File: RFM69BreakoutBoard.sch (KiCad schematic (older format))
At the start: 22 parts, among them P1 CONN_7, P10 TST, P2 TST, P3 TST, P4 TST, P5 TST, P6 TST, P7 TST, P8 TST, P9 TST, U1 MCP1703, U2 74LVC245, U3 RFM69HW

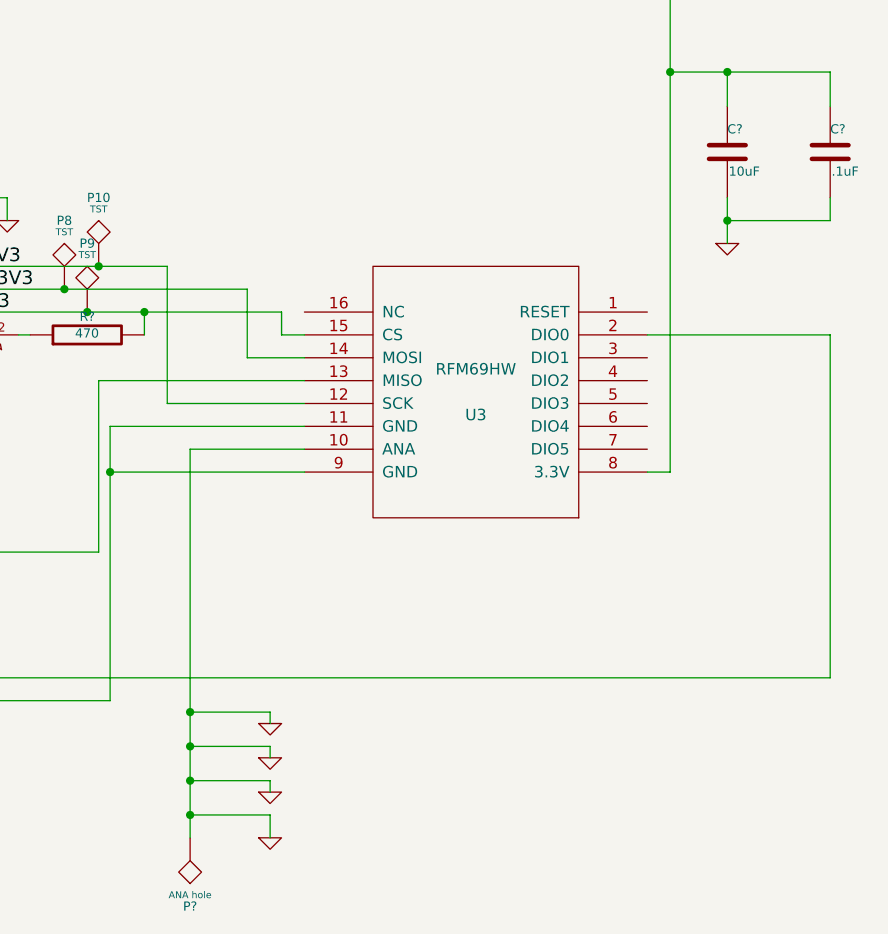
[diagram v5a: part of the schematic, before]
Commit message: changed cap near rfm69hw to 47uF, modified ANA pin
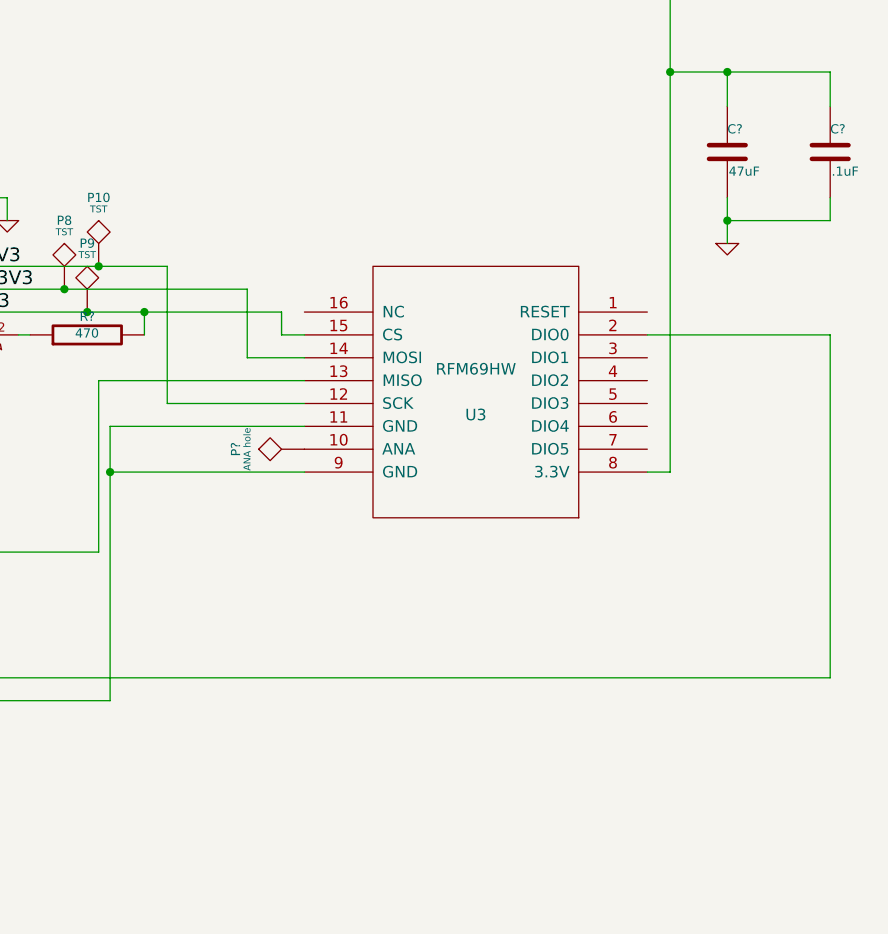
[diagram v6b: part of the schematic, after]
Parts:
- C?: value 10uF -> 47uF
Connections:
- wire segments 89 -> 79
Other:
- moved on the sheet: P?
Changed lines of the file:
@@
 P 10100 3650
 F 0 "C?" H 10100 3750 40  0000 L CNN
-F 1 "10uF" H 10106 3565 40  0000 L CNN
+F 1 "47uF" H 10106 3565 40  0000 L CNN
 F 2 "~" H 10138 3500 30  0000 C CNN
 F 3 "~" H 10100 3650 60  0000 C CNN
@@
 L TST P?
 U 1 1 530E5A0D
-P 7750 6650
-F 0 "P?" H 7750 6950 40  0000 C CNN
-F 1 "ANA hole" H 7750 6900 30  0000 C CNN
-F 2 "~" H 7750 6650 60  0000 C CNN
-F 3 "~" H 7750 6650 60  0000 C CNN
-	1    7750 6650
-	-1   0    0    1
-$EndComp
-Wire Wire Line
-	8250 4950 7750 4950
-Wire Wire Line
-	7750 4950 7750 6650
-$Comp
-L GND #PWR?
-U 1 1 530E5AC0
-P 8100 6450
-F 0 "#PWR?" H 8100 6450 30  0001 C CNN
-F 1 "GND" H 8100 6380 30  0001 C CNN
-F 2 "" H 8100 6450 60  0000 C CNN
-F 3 "" H 8100 6450 60  0000 C CNN
-	1    8100 6450
-	1    0    0    -1
-$EndComp
-Wire Wire Line
-	7750 6400 8100 6400
-Wire Wire Line
-	8100 6400 8100 6450
-Connection ~ 7750 6400
-$Comp
-L GND #PWR?
-U 1 1 530E5B36
-P 8100 6300
-F 0 "#PWR?" H 8100 6300 30  0001 C CNN
-F 1 "GND" H 8100 6230 30  0001 C CNN
-F 2 "" H 8100 6300 60  0000 C CNN
-F 3 "" H 8100 6300 60  0000 C CNN
-	1    8100 6300
-	1    0    0    -1
-$EndComp
-Wire Wire Line
-	7750 6250 8100 6250
-Connection ~ 7750 6250
-$Comp
-L GND #PWR?
-U 1 1 530E5BAF
-P 8100 6150
-F 0 "#PWR?" H 8100 6150 30  0001 C CNN
-F 1 "GND" H 8100 6080 30  0001 C CNN
-F 2 "" H 8100 6150 60  0000 C CNN
-F 3 "" H 8100 6150 60  0000 C CNN
-	1    8100 6150
-	1    0    0    -1
-$EndComp
-Wire Wire Line
-	7750 6100 8100 6100
-Connection ~ 7750 6100
-Wire Wire Line
-	8100 6100 8100 6150
-Wire Wire Line
-	8100 6250 8100 6300
-$Comp
-L GND #PWR?
-U 1 1 530E5DE4
-P 8100 6650
-F 0 "#PWR?" H 8100 6650 30  0001 C CNN
-F 1 "GND" H 8100 6580 30  0001 C CNN
-F 2 "" H 8100 6650 60  0000 C CNN
-F 3 "" H 8100 6650 60  0000 C CNN
-	1    8100 6650
-	1    0    0    -1
-$EndComp
-Wire Wire Line
-	7750 6550 8100 6550
-Wire Wire Line
-	8100 6550 8100 6650
-Connection ~ 7750 6550
+P 8250 4950
+F 0 "P?" H 8250 5250 40  0000 C CNN
+F 1 "ANA hole" H 8250 5200 30  0000 C CNN
+F 2 "~" H 8250 4950 60  0000 C CNN
+F 3 "~" H 8250 4950 60  0000 C CNN
+	1    8250 4950
+	0    -1   -1   0
+$EndComp
 $EndSCHEMATC

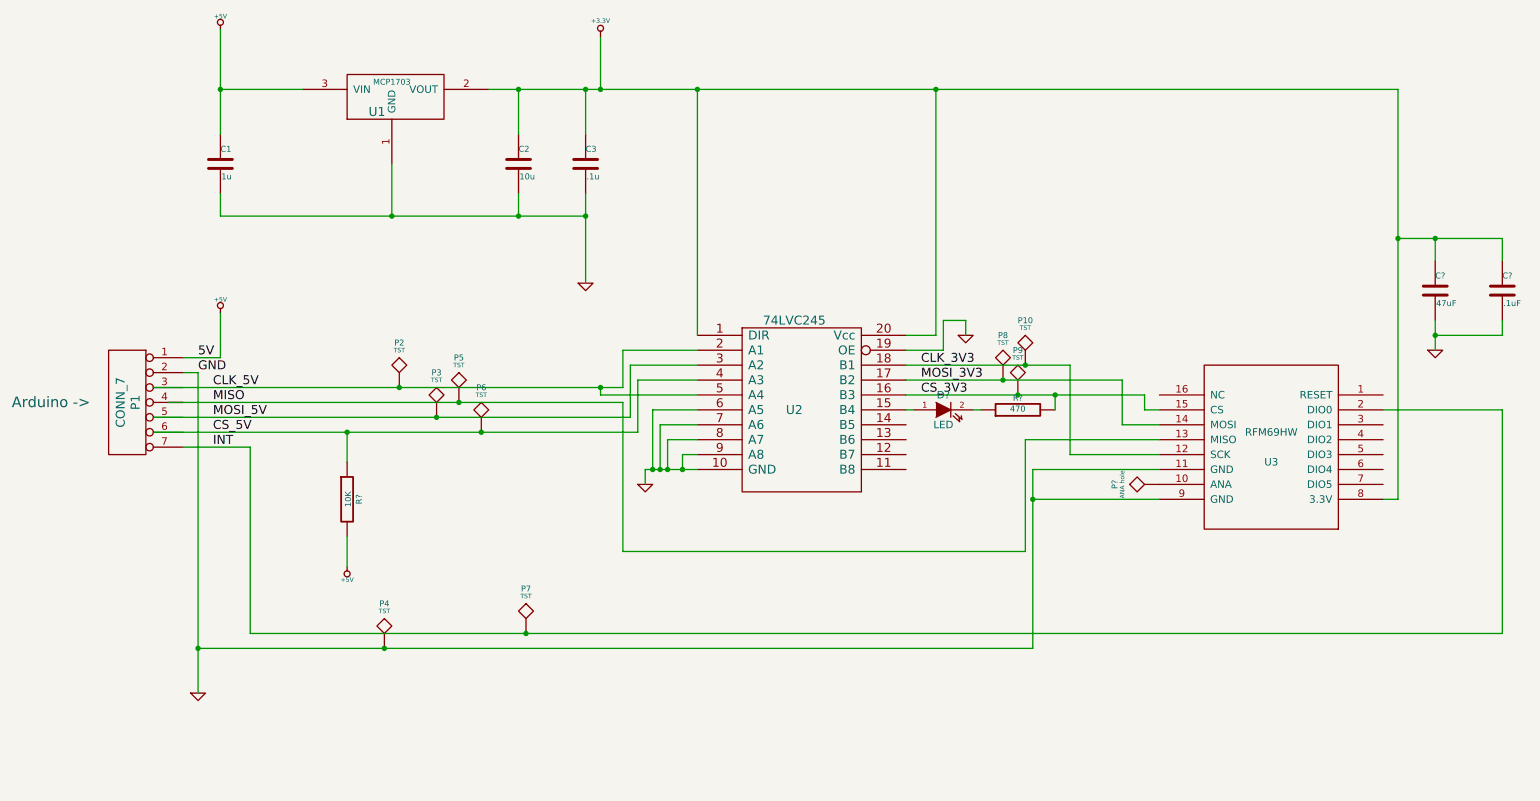
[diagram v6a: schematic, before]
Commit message: replaced larger caps to be electrolytic caps in the schematic
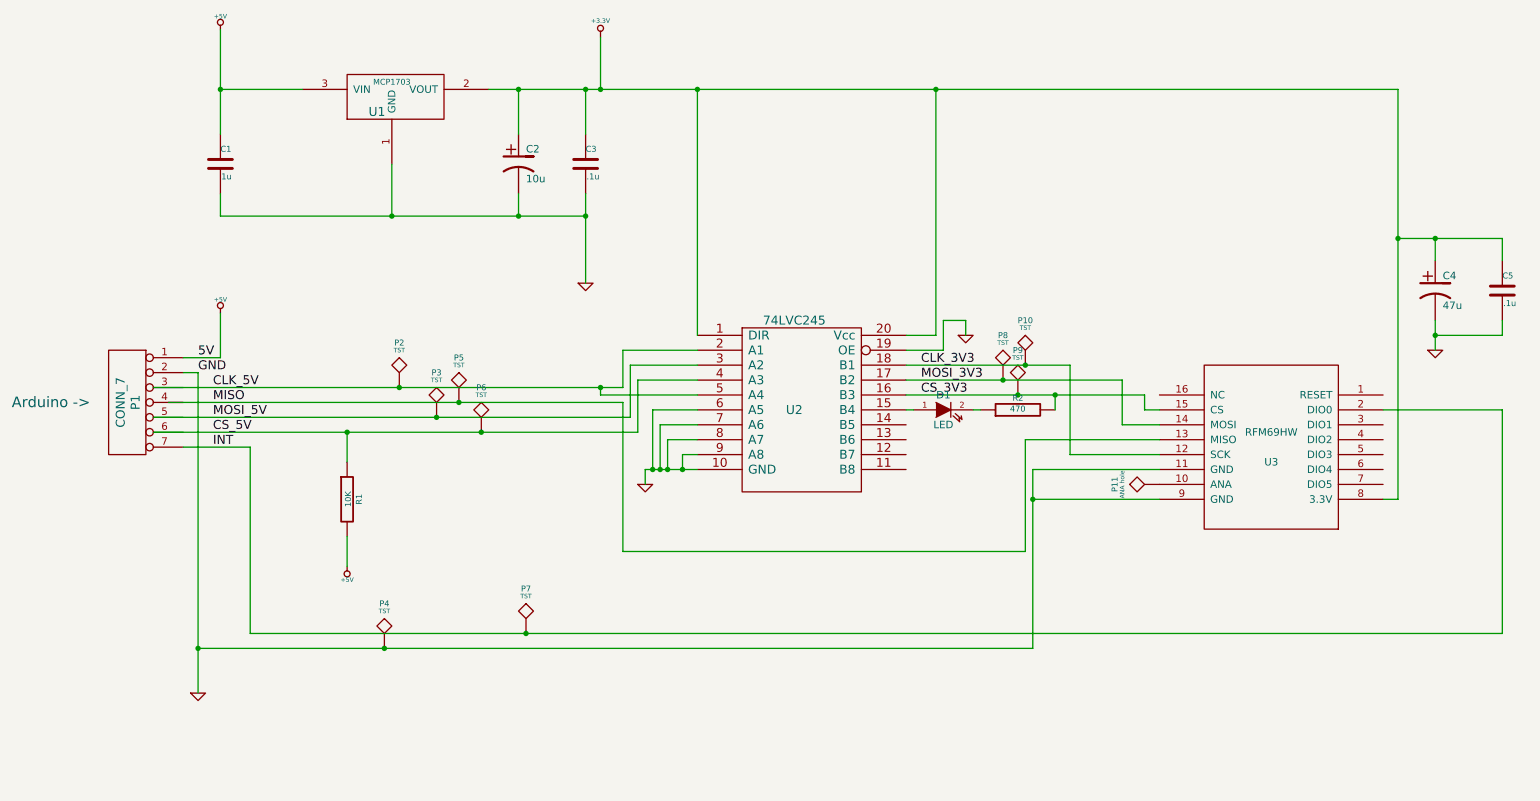
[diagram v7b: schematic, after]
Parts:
- removed C2: 10u, ~, symbol C
- removed C?: 47uF, ~, symbol C
- added C2: 10u, ~, symbol CP1
- added C4: 47u, ~, symbol CP1
- C5: renamed from C?; value .1uF -> .1u
- gave numbers to parts that had none: 4
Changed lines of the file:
@@
 Sheet 1 1
 Title ""
-Date "26 feb 2014"
+Date "27 feb 2014"
 Rev ""
 Comp ""
@@
 $EndComp
 $Comp
-L C C2
-U 1 1 5305B2AF
-P 3950 2800
-F 0 "C2" H 3950 2900 40  0000 L CNN
-F 1 "10u" H 3956 2715 40  0000 L CNN
-F 2 "~" H 3988 2650 30  0000 C CNN
-F 3 "~" H 3950 2800 60  0000 C CNN
-F 4 "Yageo" H 3950 2800 60  0001 C CNN "MFG Name"
-F 5 "CC0805ZKY5V6BB106" H 3950 2800 60  0001 C CNN "MFG Part Number"
-F 6 "311-1355-1-ND" H 3950 2800 60  0001 C CNN "Distributor Part Number"
-F 7 "http://www.digikey.com/product-detail/en/CC0805ZKY5V6BB106/311-1355-1-ND/2103139" H 3950 2800 60  0001 C CNN "Distributor Part Number Link"
-	1    3950 2800
-	1    0    0    -1
-$EndComp
-$Comp
 L C C3
 U 1 1 5305B2B5
@@
 $EndComp
 $Comp
-L +3.3V #PWR5
+L +3.3V #PWR6
 U 1 1 5305B30B
 P 4500 1950
-F 0 "#PWR5" H 4500 1910 30  0001 C CNN
+F 0 "#PWR6" H 4500 1910 30  0001 C CNN
 F 1 "+3.3V" H 4500 2060 30  0000 C CNN
 F 2 "" H 4500 1950 60  0000 C CNN
@@
 $EndComp
 $Comp
-L GND #PWR4
+L GND #PWR5
 U 1 1 5305B481
 P 4400 3600
-F 0 "#PWR4" H 4400 3600 30  0001 C CNN
+F 0 "#PWR5" H 4400 3600 30  0001 C CNN
 F 1 "GND" H 4400 3530 30  0001 C CNN
 F 2 "" H 4400 3600 60  0000 C CNN
@@
 CS_3V3
 $Comp
-L GND #PWR6
+L GND #PWR7
 U 1 1 530BB7C1
 P 4800 4950
-F 0 "#PWR6" H 4800 4950 30  0001 C CNN
+F 0 "#PWR7" H 4800 4950 30  0001 C CNN
 F 1 "GND" H 4800 4880 30  0001 C CNN
 F 2 "" H 4800 4950 60  0000 C CNN
@@
 CLK_5V
 $Comp
-L GND #PWR7
+L GND #PWR8
 U 1 1 530BC03D
 P 6950 3950
-F 0 "#PWR7" H 6950 3950 30  0001 C CNN
+F 0 "#PWR8" H 6950 3950 30  0001 C CNN
 F 1 "GND" H 6950 3880 30  0001 C CNN
 F 2 "" H 6950 3950 60  0000 C CNN
@@
 $EndComp
 $Comp
-L R R?
+L R R2
 U 1 1 530DC938
 P 7300 4450
-F 0 "R?" V 7380 4450 40  0000 C CNN
+F 0 "R2" V 7380 4450 40  0000 C CNN
 F 1 "470" V 7307 4451 40  0000 C CNN
 F 2 "~" V 7230 4450 30  0000 C CNN
@@
 $EndComp
 $Comp
-L LED D?
+L LED D1
 U 1 1 530DC956
 P 6800 4450
-F 0 "D?" H 6800 4550 50  0000 C CNN
+F 0 "D1" H 6800 4550 50  0000 C CNN
 F 1 "LED" H 6800 4350 50  0000 C CNN
 F 2 "~" H 6800 4450 60  0000 C CNN
@@
 $EndComp
 $Comp
-L R R?
+L R R1
 U 1 1 530DCC1C
 P 2800 5050
-F 0 "R?" V 2880 5050 40  0000 C CNN
+F 0 "R1" V 2880 5050 40  0000 C CNN
 F 1 "10K" V 2807 5051 40  0000 C CNN
 F 2 "~" V 2730 5050 30  0000 C CNN
@@
 $EndComp
 $Comp
-L +5V #PWR?
+L +5V #PWR4
 U 1 1 530DCD57
 P 2800 5500
-F 0 "#PWR?" H 2800 5590 20  0001 C CNN
+F 0 "#PWR4" H 2800 5590 20  0001 C CNN
 F 1 "+5V" H 2800 5590 30  0000 C CNN
 F 2 "" H 2800 5500 60  0000 C CNN
@@
 $EndComp
 $Comp
-L C C?
-U 1 1 530DFDC0
-P 10100 3650
-F 0 "C?" H 10100 3750 40  0000 L CNN
-F 1 "47uF" H 10106 3565 40  0000 L CNN
-F 2 "~" H 10138 3500 30  0000 C CNN
-F 3 "~" H 10100 3650 60  0000 C CNN
-	1    10100 3650
-	1    0    0    -1
-$EndComp
-$Comp
-L GND #PWR?
+L GND #PWR9
 U 1 1 530DFEA1
 P 10100 4050
-F 0 "#PWR?" H 10100 4050 30  0001 C CNN
+F 0 "#PWR9" H 10100 4050 30  0001 C CNN
 F 1 "GND" H 10100 3980 30  0001 C CNN
 F 2 "" H 10100 4050 60  0000 C CNN
@@
 $EndComp
 $Comp
-L C C?
+L C C5
 U 1 1 530DFF22
 P 10550 3650
-F 0 "C?" H 10550 3750 40  0000 L CNN
-F 1 ".1uF" H 10556 3565 40  0000 L CNN
+F 0 "C5" H 10550 3750 40  0000 L CNN
+F 1 ".1u" H 10556 3565 40  0000 L CNN
 F 2 "~" H 10588 3500 30  0000 C CNN
 F 3 "~" H 10550 3650 60  0000 C CNN
@@
 Connection ~ 10100 3300
 $Comp
-L TST P?
+L TST P11
 U 1 1 530E5A0D
 P 8250 4950
-F 0 "P?" H 8250 5250 40  0000 C CNN
+F 0 "P11" H 8250 5250 40  0000 C CNN
 F 1 "ANA hole" H 8250 5200 30  0000 C CNN
 F 2 "~" H 8250 4950 60  0000 C CNN
@@
 	0    -1   -1   0
 $EndComp
+$Comp
+L CP1 C4
+U 1 1 530F2E03
+P 10100 3650
+F 0 "C4" H 10150 3750 50  0000 L CNN
+F 1 "47u" H 10150 3550 50  0000 L CNN
+F 2 "~" H 10100 3650 60  0000 C CNN
+F 3 "~" H 10100 3650 60  0000 C CNN
+	1    10100 3650
+	1    0    0    -1
+$EndComp
+$Comp
+L CP1 C2
+U 1 1 530F2E4A
+P 3950 2800
+F 0 "C2" H 4000 2900 50  0000 L CNN
+F 1 "10u" H 4000 2700 50  0000 L CNN
+F 2 "~" H 3950 2800 60  0000 C CNN
+F 3 "~" H 3950 2800 60  0000 C CNN
+	1    3950 2800
+	1    0    0    -1
+$EndComp
 $EndSCHEMATC

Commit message: updated schema: changed 47uF cap to 10uF. Changed test point symbol
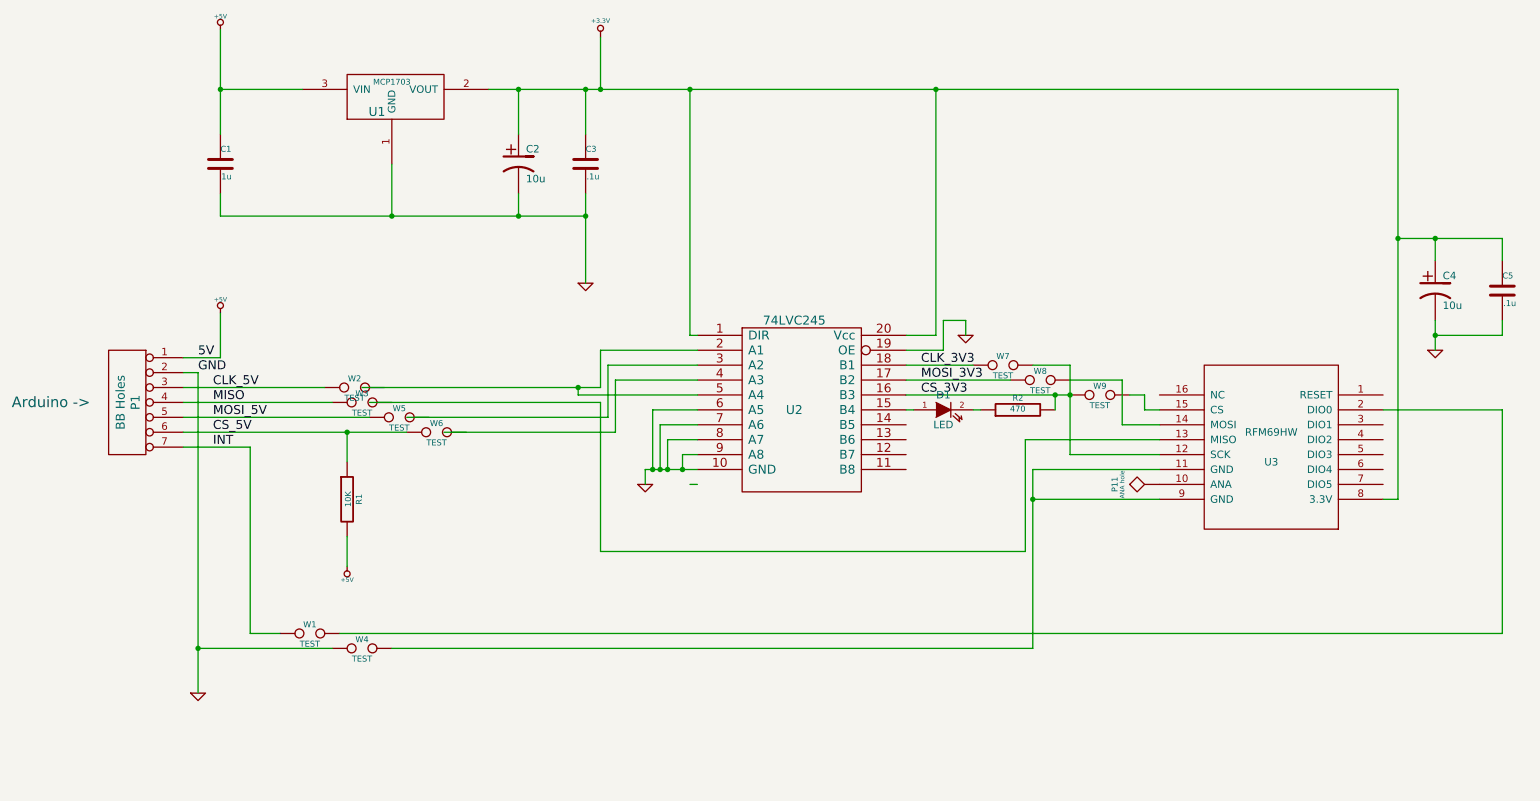
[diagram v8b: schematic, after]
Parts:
- removed P10, P2, P3, P4, P5, P6, P7, P8, P9: TST, ~, symbol TST
- added W1, W2, W3, W4, W5, W6, W7, W8, W9: TEST, ~, symbol TEST
- C4: value 47u -> 10u
- P1: value CONN_7 -> BB Holes
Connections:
- wire segments 79 -> 90
